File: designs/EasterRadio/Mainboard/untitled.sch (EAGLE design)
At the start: 47 parts, among them IC1 Analog Digital, IC2 74HC595D, IC3 74HC595D, IC4 74HC595D

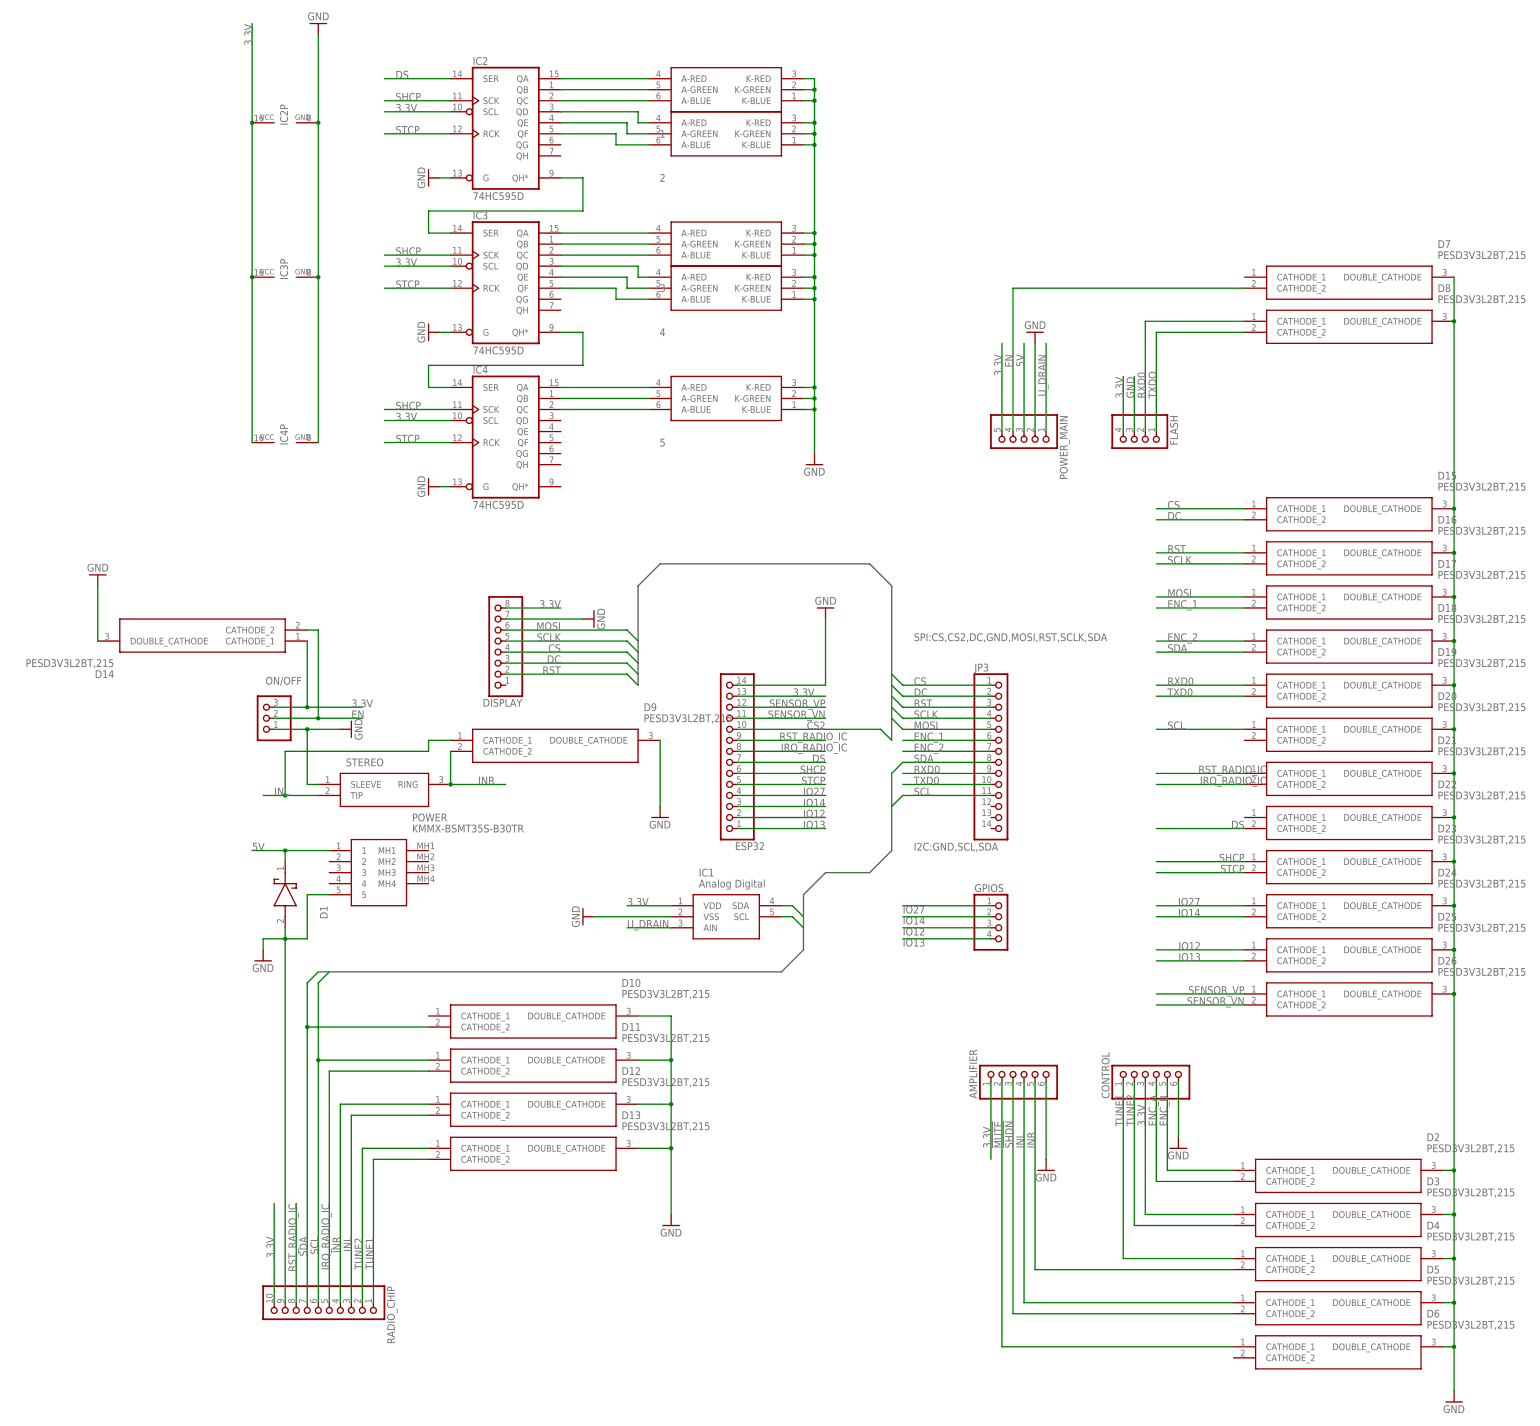
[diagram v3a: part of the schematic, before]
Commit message: finalzed brd layout main pcb
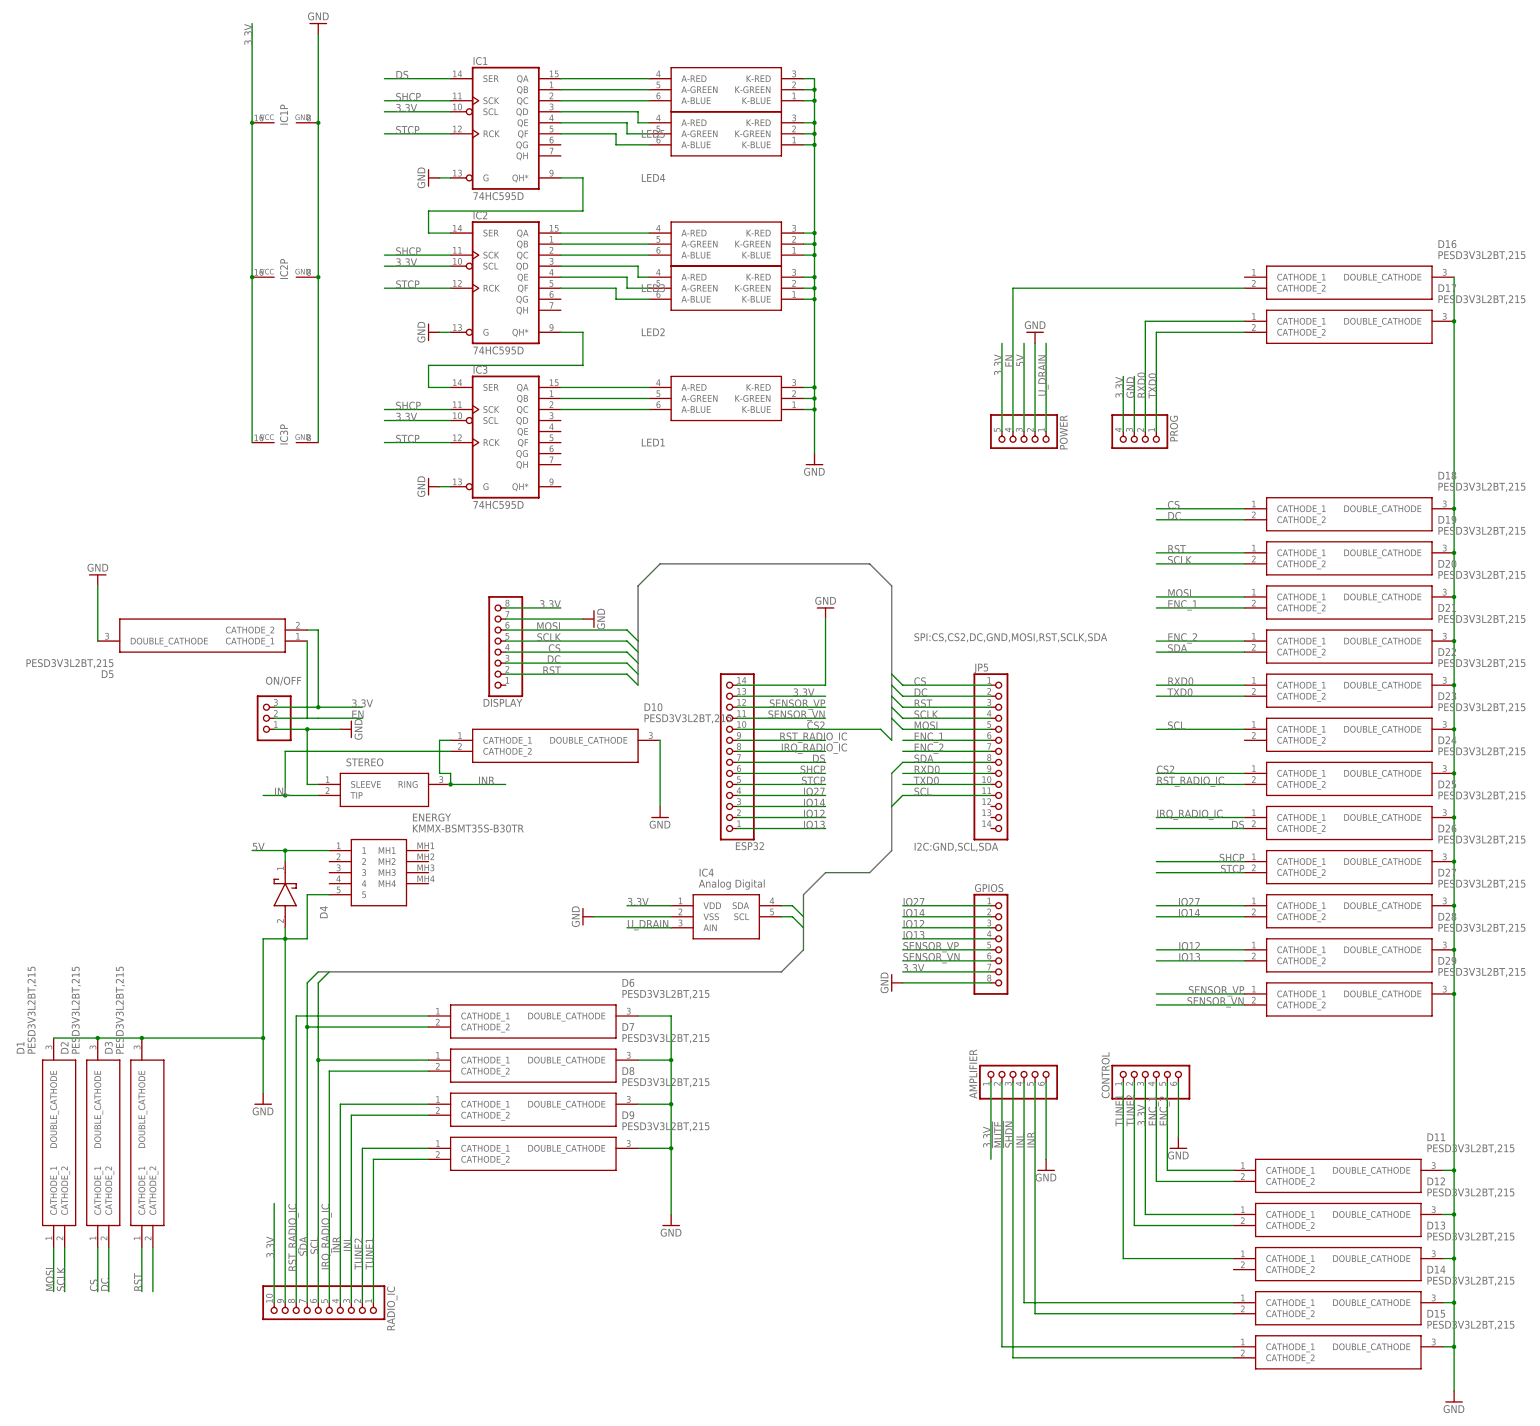
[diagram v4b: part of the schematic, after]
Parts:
- removed POWER_MAIN: (no value), pinhead:PINHD-1X5
- added D27, D28, D29: PESD3V3L2BT,215, MouserUseful:PESD3V3L2BT,215
- added ENERGY: KMMX-BSMT35S-B30TR, MouserUseful:KMMX-BSMT35S-B30TR
- D1: value LSM115JE3_TR13 -> PESD3V3L2BT,215; device CommonParts:LSM115JE3_TR13 -> MouserUseful:PESD3V3L2BT,215
- D4: value PESD3V3L2BT,215 -> LSM115JE3_TR13; device MouserUseful:PESD3V3L2BT,215 -> CommonParts:LSM115JE3_TR13
- GPIOS: device pinhead:PINHD-1X4 -> pinhead:PINHD-1X8
- IC1: value Analog Digital -> 74HC595D; device MouserUseful:MCP3221A6T-E_OTVAO -> NixieTube:74HC595D
- IC4: value 74HC595D -> Analog Digital; device NixieTube:74HC595D -> MouserUseful:MCP3221A6T-E_OTVAO
- POWER: value KMMX-BSMT35S-B30TR -> (none); device MouserUseful:KMMX-BSMT35S-B30TR -> pinhead:PINHD-1X5
- renumbered 1 to LED5, 2 to LED4, 3 to LED3, 4 to LED2, 5 to LED1, FLASH to PROG, JP3 to JP5, RADIO_CHIP to RADIO_IC
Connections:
- removed net ENC_A: CONTROL.4, D2.CATHODE_2
- removed net ENC_B: CONTROL.5, D2.CATHODE_1
- removed net N$21 (its old number): IC3A.QH*, IC4A.SER
- removed net TXDO: D8.CATHODE_2, PROG.1
- new net N$17: IC1A.QH*, IC2A.SER
- new net N$5: D3.CATHODE_2
- net !MUTE: now also D15.CATHODE_1; no longer D6.CATHODE_1
- net !SHDN: now also D15.CATHODE_2; no longer D5.CATHODE_2
- net 3.3V: now also D12.CATHODE_1, D5.CATHODE_2, GPIOS.7, IC1A.SCL, IC1P.VCC, IC4.VDD, POWER.5; no longer D14.CATHODE_1, D3.CATHODE_1, IC1.VDD, IC4A.SCL, IC4P.VCC, POWER_MAIN.5
- net 5V: now also D4.K, ENERGY.1, POWER.3; no longer D1.K, POWER.1, POWER_MAIN.3
- net CS: now also D18.CATHODE_1, D2.CATHODE_1; no longer D15.CATHODE_1
- net CS2: now also D24.CATHODE_1
- net DC: now also D18.CATHODE_2, D2.CATHODE_2; no longer D15.CATHODE_2
- net DS: now also D25.CATHODE_2, IC1A.SER; no longer D22.CATHODE_2, IC2A.SER
- net EN: now also D16.CATHODE_2, D5.CATHODE_1, POWER.4; no longer D14.CATHODE_2, D7.CATHODE_2, POWER_MAIN.4
- net ENC_1: now also CONTROL.4, D11.CATHODE_2, D20.CATHODE_2; no longer D17.CATHODE_2
- net ENC_2: now also CONTROL.5, D11.CATHODE_1, D21.CATHODE_1; no longer D18.CATHODE_1
- net GND: now also D1.DOUBLE_CATHODE, D27.DOUBLE_CATHODE, D28.DOUBLE_CATHODE, D29.DOUBLE_CATHODE, D4.A, ENERGY.5, GPIOS.8, IC1A.G, IC1P.GND, IC4.VSS, POWER.2; no longer D1.A, D4.DOUBLE_CATHODE, IC1.VSS, IC4A.G, IC4P.GND, POWER.5, POWER_MAIN.2
- net INL: now also D10.CATHODE_2, D14.CATHODE_1, D8.CATHODE_2; no longer D12.CATHODE_2, D5.CATHODE_1, D9.CATHODE_1
- net INR: now also D10.CATHODE_1, D14.CATHODE_2, D8.CATHODE_1; no longer D12.CATHODE_1, D4.CATHODE_2, D9.CATHODE_2
- net IO12: now also D28.CATHODE_1; no longer D25.CATHODE_1
- net IO13: now also D28.CATHODE_2; no longer D25.CATHODE_2
- net IO14: now also D27.CATHODE_2; no longer D24.CATHODE_2
- net IO27: now also D27.CATHODE_1; no longer D24.CATHODE_1
- net IRQ_RADIO_IC: now also D25.CATHODE_1, D7.CATHODE_2; no longer D11.CATHODE_2, D21.CATHODE_2
- net MOSI: now also D1.CATHODE_1, D20.CATHODE_1; no longer D17.CATHODE_1
- net N$10: now also IC1A.QD; no longer IC2A.QD
- net N$11: now also IC1A.QE; no longer IC2A.QE
- net N$12: now also IC1A.QF; no longer IC2A.QF
- net N$13: now also IC2A.QA; no longer IC3A.QA
- net N$14: now also IC2A.QB; no longer IC3A.QB
- net N$15: now also IC2A.QD; no longer IC3A.QD
- net N$16: now also IC2A.QE; no longer IC3A.QE
- net N$18: now also IC3A.QA; no longer IC4A.QA
- net N$19: now also IC3A.QB; no longer IC4A.QB
- net N$3: now also IC2A.QC; no longer IC3A.QC
- net N$4: now also IC3A.QC; no longer IC4A.QC
- net N$6: now also IC2A.QF; no longer IC3A.QF
- net N$7: now also IC1A.QA; no longer IC2A.QA
- net N$8: now also IC1A.QB; no longer IC2A.QB
- net N$9: now also IC1A.QC; no longer IC2A.QC
- net RST: now also D19.CATHODE_1, D3.CATHODE_1; no longer D16.CATHODE_1
- net RST_RADIO_IC: now also D24.CATHODE_2, D6.CATHODE_1; no longer D21.CATHODE_1
- net RXD0: now also D17.CATHODE_1, D22.CATHODE_1; no longer D19.CATHODE_1, D8.CATHODE_1
- net SCL: now also D23.CATHODE_1, D7.CATHODE_1, IC4.SCL; no longer D11.CATHODE_1, D20.CATHODE_1, IC1.SCL
- net SCLK: now also D1.CATHODE_2, D19.CATHODE_2; no longer D16.CATHODE_2
- net SDA: now also D21.CATHODE_2, D6.CATHODE_2, IC4.SDA; no longer D10.CATHODE_2, D18.CATHODE_2, IC1.SDA
- net SENSOR_VN: now also D29.CATHODE_2, GPIOS.6; no longer D26.CATHODE_2
- net SENSOR_VP: now also D29.CATHODE_1, GPIOS.5; no longer D26.CATHODE_1
- net SHCP: now also D26.CATHODE_1, IC1A.SCK; no longer D23.CATHODE_1, IC4A.SCK
- net STCP: now also D26.CATHODE_2, IC1A.RCK; no longer D23.CATHODE_2, IC4A.RCK
- net TUNE1: now also D13.CATHODE_1, D9.CATHODE_2; no longer D13.CATHODE_2, D4.CATHODE_1
- net TUNE2: now also D12.CATHODE_2, D9.CATHODE_1; no longer D13.CATHODE_1, D3.CATHODE_2
- net TXD0: now also D17.CATHODE_2, D22.CATHODE_2, PROG.1; no longer D19.CATHODE_2
- net U_DRAIN: now also IC4.AIN, POWER.1; no longer IC1.AIN, POWER_MAIN.1
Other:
- moved on the sheet: D10, D11, D12, D13, D14, D15, D16, D17, D18, D19, D2, D20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

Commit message: final changes on mainboard
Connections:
- net !MUTE: now also D15.CATHODE_2; no longer D15.CATHODE_1
- net !SHDN: now also D15.CATHODE_1; no longer D15.CATHODE_2
- net INL: now also D14.CATHODE_2; no longer D14.CATHODE_1
- net INR: now also D14.CATHODE_1; no longer D14.CATHODE_2
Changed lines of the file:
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@@
 <pinref part="AMPLIFIER" gate="A" pin="5"/>
 <label x="248.92" y="68.58" size="1.778" layer="95" rot="R90"/>
-<wire x1="248.92" y1="83.82" x2="248.92" y2="30.48" width="0.1524" layer="91"/>
-<pinref part="D14" gate="G$1" pin="CATHODE_2"/>
-<wire x1="248.92" y1="30.48" x2="294.64" y2="30.48" width="0.1524" layer="91"/>
+<wire x1="248.92" y1="83.82" x2="248.92" y2="33.02" width="0.1524" layer="91"/>
+<pinref part="D14" gate="G$1" pin="CATHODE_1"/>
+<wire x1="294.64" y1="33.02" x2="248.92" y2="33.02" width="0.1524" layer="91"/>
 </segment>
 <segment>
@@
 <pinref part="AMPLIFIER" gate="A" pin="4"/>
 <label x="246.38" y="68.58" size="1.778" layer="95" rot="R90"/>
-<wire x1="246.38" y1="83.82" x2="246.38" y2="33.02" width="0.1524" layer="91"/>
-<pinref part="D14" gate="G$1" pin="CATHODE_1"/>
-<wire x1="246.38" y1="33.02" x2="294.64" y2="33.02" width="0.1524" layer="91"/>
+<wire x1="246.38" y1="83.82" x2="246.38" y2="30.48" width="0.1524" layer="91"/>
+<pinref part="D14" gate="G$1" pin="CATHODE_2"/>
+<wire x1="294.64" y1="30.48" x2="246.38" y2="30.48" width="0.1524" layer="91"/>
 </segment>
 <segment>
@@
 <pinref part="AMPLIFIER" gate="A" pin="2"/>
 <label x="241.3" y="68.58" size="1.778" layer="95" rot="R90"/>
-<wire x1="241.3" y1="83.82" x2="241.3" y2="22.86" width="0.1524" layer="91"/>
-<pinref part="D15" gate="G$1" pin="CATHODE_1"/>
-<wire x1="294.64" y1="22.86" x2="241.3" y2="22.86" width="0.1524" layer="91"/>
+<wire x1="241.3" y1="83.82" x2="241.3" y2="20.32" width="0.1524" layer="91"/>
+<pinref part="D15" gate="G$1" pin="CATHODE_2"/>
+<wire x1="294.64" y1="20.32" x2="241.3" y2="20.32" width="0.1524" layer="91"/>
 </segment>
 </net>
@@
 <pinref part="AMPLIFIER" gate="A" pin="3"/>
 <label x="243.84" y="68.58" size="1.778" layer="95" rot="R90"/>
-<wire x1="243.84" y1="83.82" x2="243.84" y2="20.32" width="0.1524" layer="91"/>
-<pinref part="D15" gate="G$1" pin="CATHODE_2"/>
-<wire x1="243.84" y1="20.32" x2="294.64" y2="20.32" width="0.1524" layer="91"/>
+<wire x1="243.84" y1="83.82" x2="243.84" y2="22.86" width="0.1524" layer="91"/>
+<pinref part="D15" gate="G$1" pin="CATHODE_1"/>
+<wire x1="294.64" y1="22.86" x2="243.84" y2="22.86" width="0.1524" layer="91"/>
 </segment>
 </net>
